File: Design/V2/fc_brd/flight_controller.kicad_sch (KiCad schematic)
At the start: 45 parts, among them U1 STM32H747BIT6

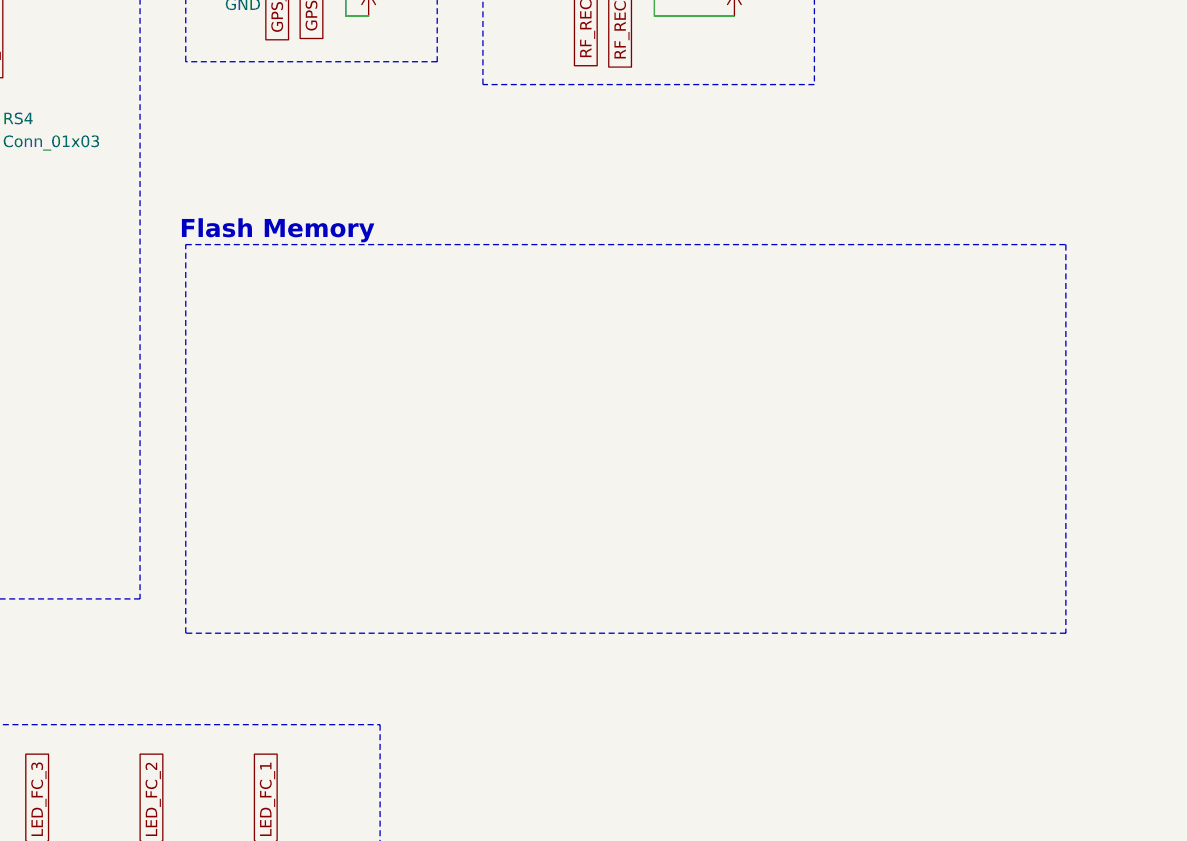
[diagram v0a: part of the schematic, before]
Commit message: added flash device
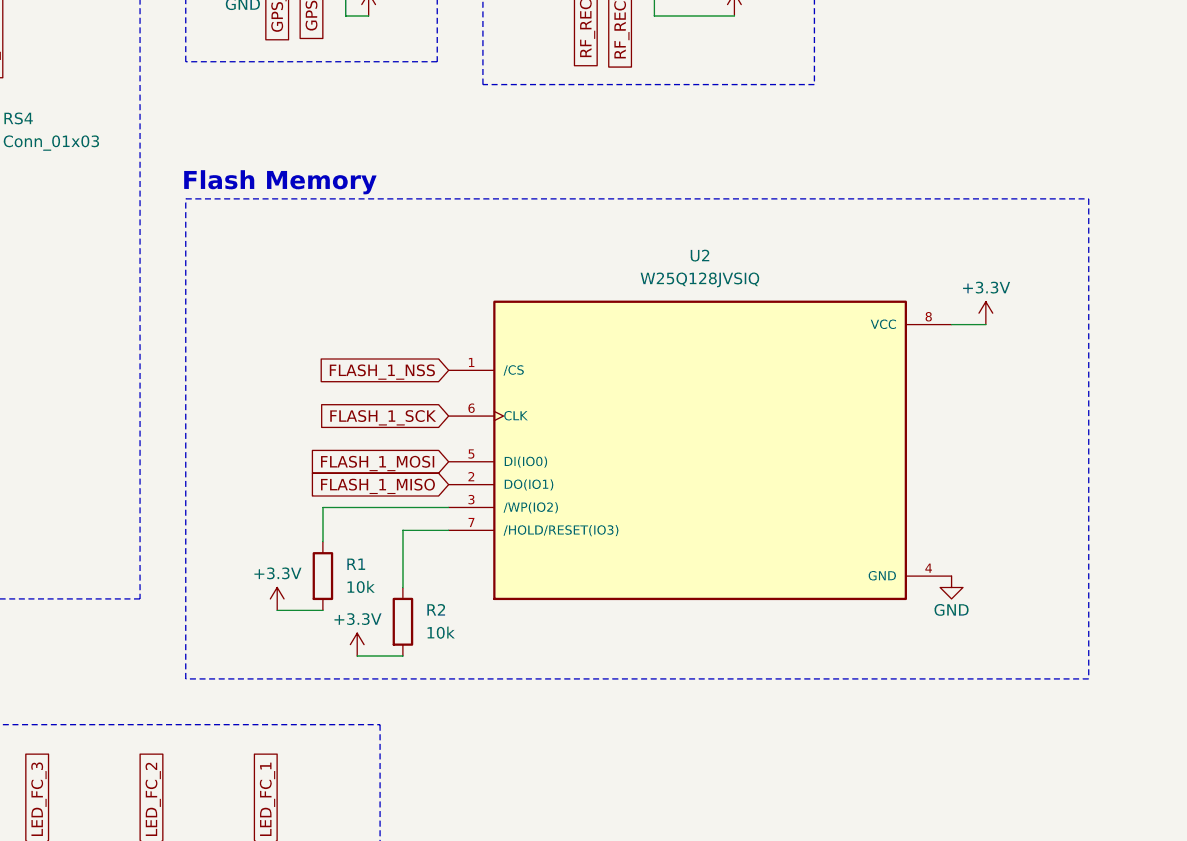
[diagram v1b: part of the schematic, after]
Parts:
- added R1, R2: 10k, Resistor_SMD:R_0603_1608Metric_Pad0.98x0.95mm_HandSolder, symbol Device:R
- added U2: W25Q128JVSIQ, W25Q128JVSIQ:SOIC127P790X216-8N, symbol W25Q128JVSIQ:W25Q128JVSIQ
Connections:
- net +3.3V: now also R1.2, R2.2, U2.8 (VCC)
- net FLASH_1_MISO: now also U2.2 (DO(IO1))
- net FLASH_1_MOSI: now also U2.5 (DI(IO0))
- net FLASH_1_NSS: now also U2.1 (/CS)
- net FLASH_1_SCK: now also U2.6 (CLK)
- net GND: now also U2.4 (GND)
- new net: R1.1, U2.3 (/WP(IO2))
- new net: R2.1, U2.7 (/HOLD/RESET(IO3))

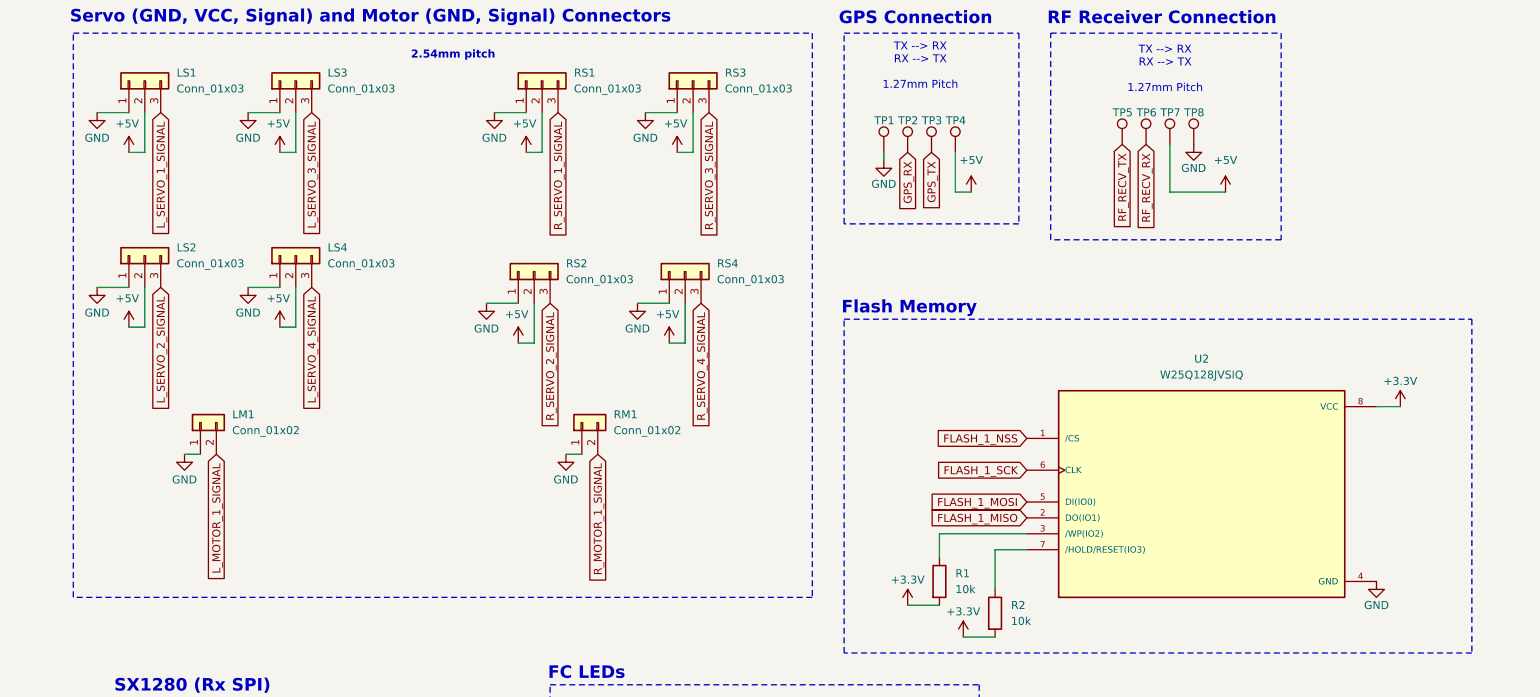
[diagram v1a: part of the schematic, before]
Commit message: layout changed to main fc board
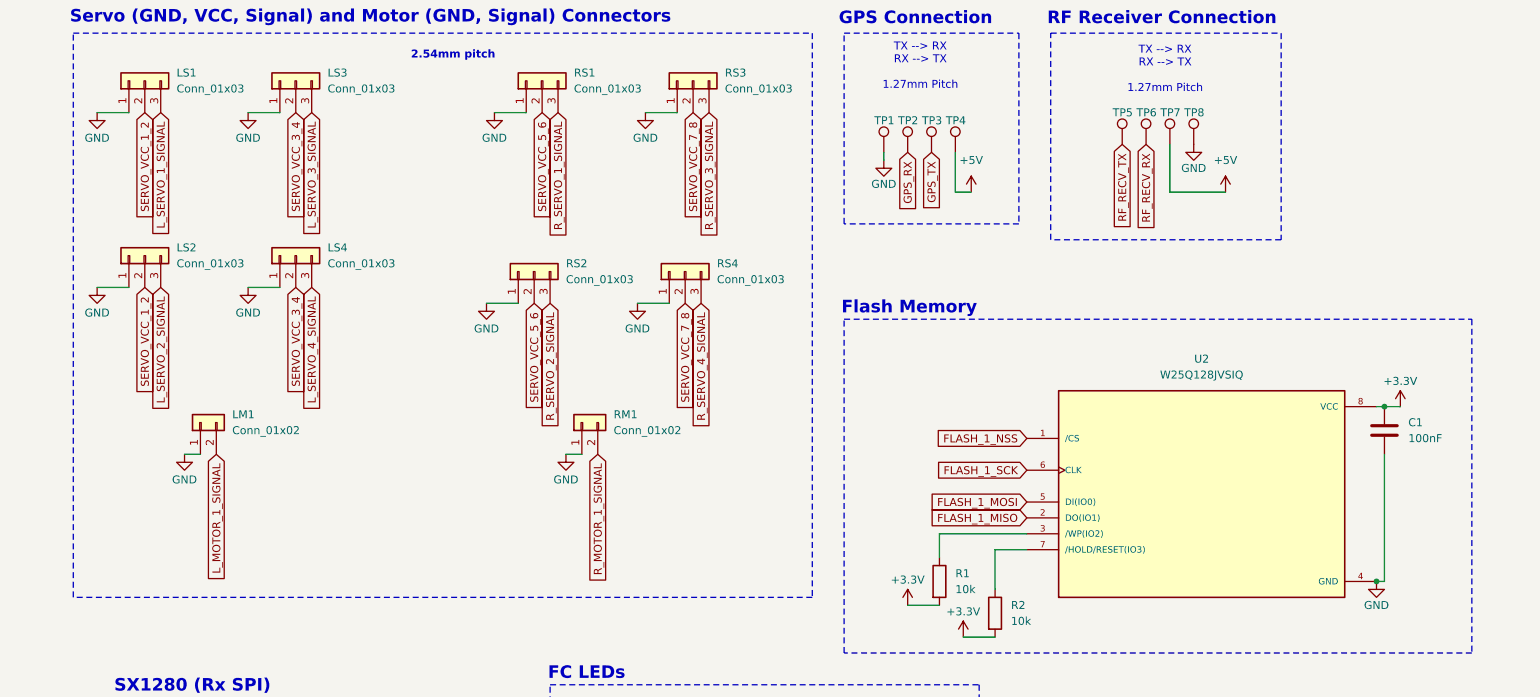
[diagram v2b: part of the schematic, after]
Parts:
- added C1: 100nF, Capacitor_SMD:C_0603_1608Metric_Pad1.08x0.95mm_HandSolder, symbol Device:C
- LM1, RM1: Manufacturer_Name JST Sales America Inc. -> (none); Manufacturer_Part_Number B2B-XH-A -> (none)
- LS1, LS2, LS3, LS4, RS1, RS2, RS3, RS4: Manufacturer_Name JST Sales America Inc. -> (none); Manufacturer_Part_Number B3B-XH-A -> (none)
- U2: footprint W25Q128JVSIQ:SOIC127P790X216-8N -> EXT_Storage:SOIC127P790X216-8N; LCSC Part # (none) -> C97521; Manufacturer_Name (none) -> Winbond Elec; Manufacturer_Part_Number (none) -> W25Q128JVSIQ
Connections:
- net +3.3V: now also C1.1
- net +5V: no longer LS1.2 (Pin_2), LS2.2 (Pin_2), LS3.2 (Pin_2), LS4.2 (Pin_2), RS1.2 (Pin_2), RS2.2 (Pin_2), RS3.2 (Pin_2), RS4.2 (Pin_2)
- net GND: now also C1.2
- new net SERVO_VCC_1_2: LS1.2 (Pin_2), LS2.2 (Pin_2)
- new net SERVO_VCC_3_4: LS3.2 (Pin_2), LS4.2 (Pin_2)
- new net SERVO_VCC_5_6: RS1.2 (Pin_2), RS2.2 (Pin_2)
- new net SERVO_VCC_7_8: RS3.2 (Pin_2), RS4.2 (Pin_2)

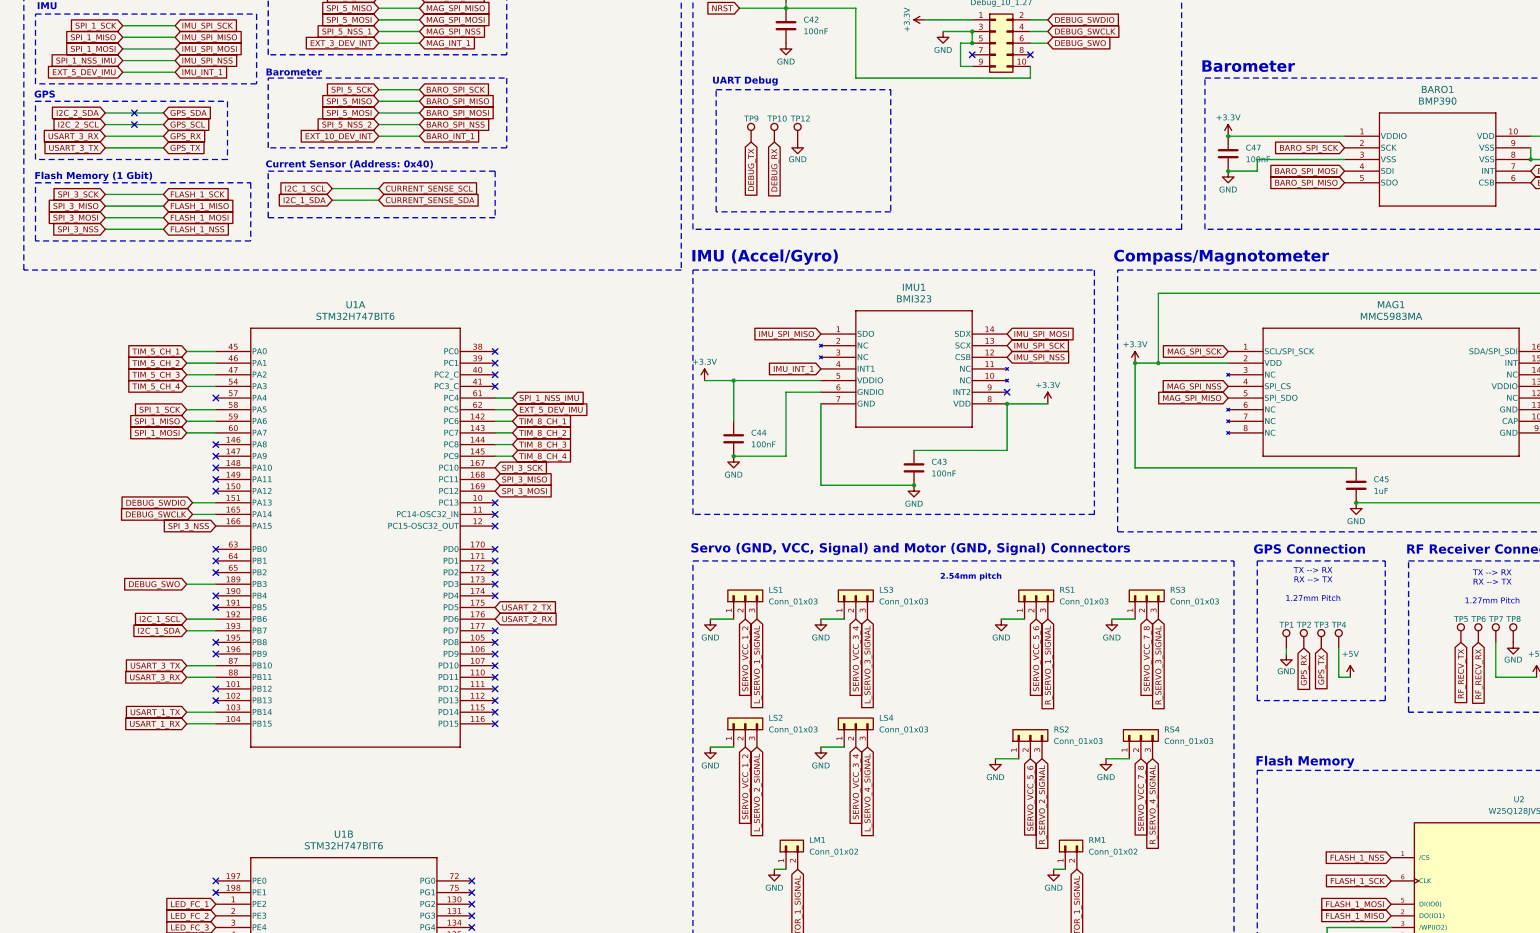
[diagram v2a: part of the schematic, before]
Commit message: completed main fc board layout
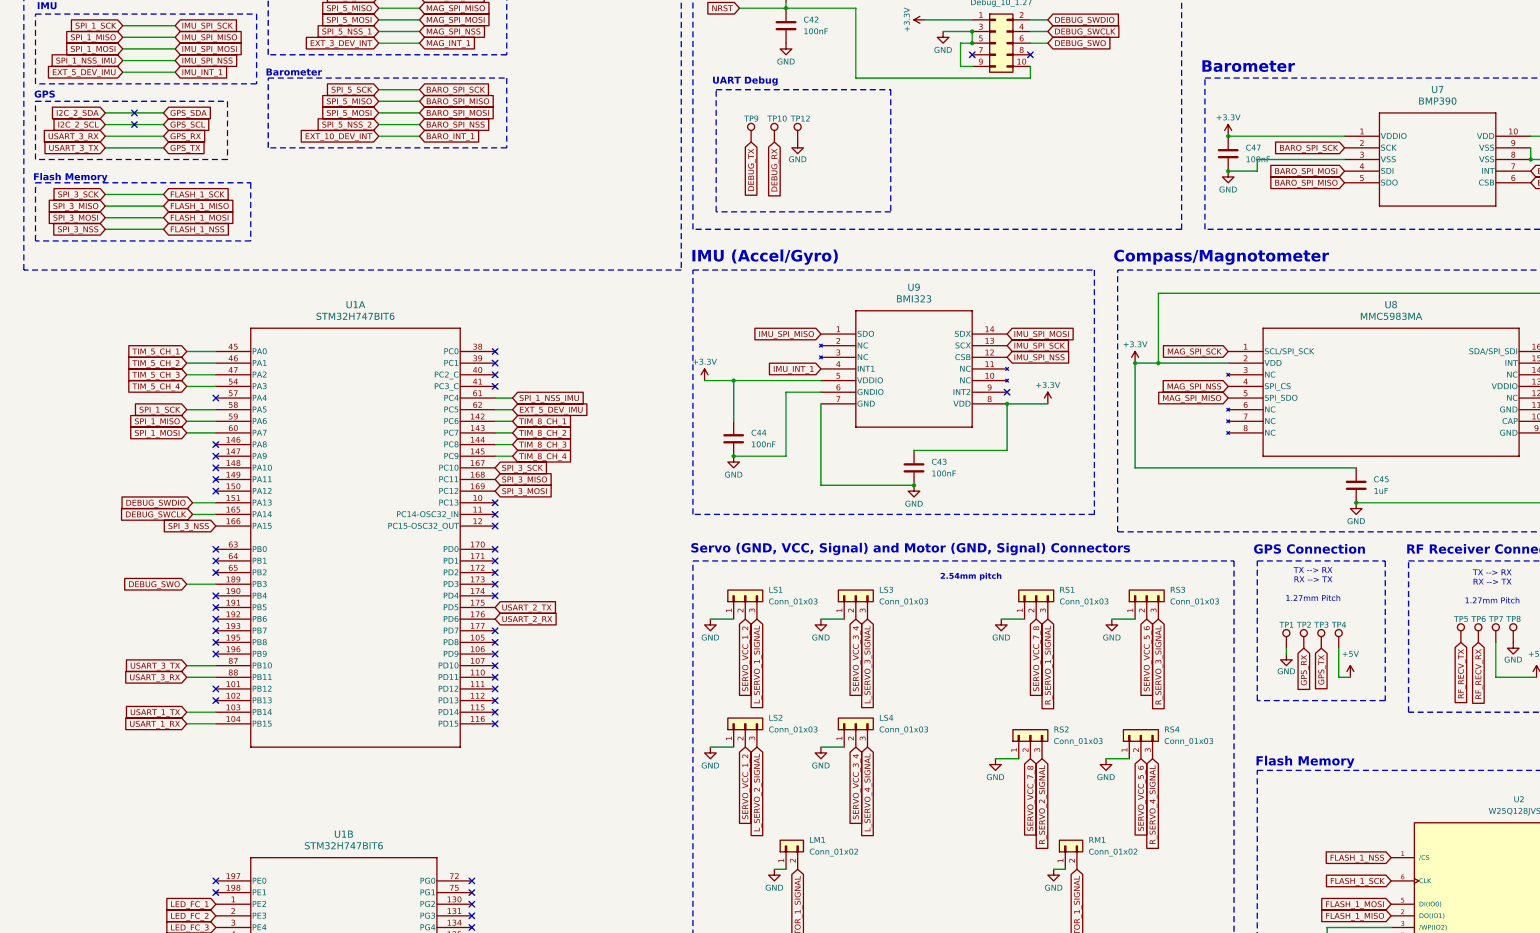
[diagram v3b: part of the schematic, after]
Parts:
- LM1, LS1, LS2, LS3, LS4, RM1, RS1, RS2, RS3, RS4, SWD1: now left out of the parts list
- R1, R2: LCSC Part # (none) -> C25804; Manufacturer_Name (none) -> UNI-ROYAL(Uniroyal Elec); Manufacturer_Part_Number (none) -> 0603WAF1002T5E
- renumbered BARO1 to U7, MAG1 to U8, IMU1 to U9
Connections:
- net SERVO_VCC_5_6: now also RS3.2 (Pin_2), RS4.2 (Pin_2); no longer RS1.2 (Pin_2), RS2.2 (Pin_2)
- net SERVO_VCC_7_8: now also RS1.2 (Pin_2), RS2.2 (Pin_2); no longer RS3.2 (Pin_2), RS4.2 (Pin_2)
- net CURRENT_SENSE_SCL: no longer names the net of U1.192 (PB6)
- net CURRENT_SENSE_SDA: no longer names the net of U1.193 (PB7)
- no-connect marks 111 -> 113
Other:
- note removed: "Current Sensor (Address: 0x40)"
- note removed: "Flash Memory (1 Gbit)"
